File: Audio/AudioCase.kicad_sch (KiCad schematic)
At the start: 3 parts, among them J1 PD給電, J2 入力ジャック, J3 出力ジャック

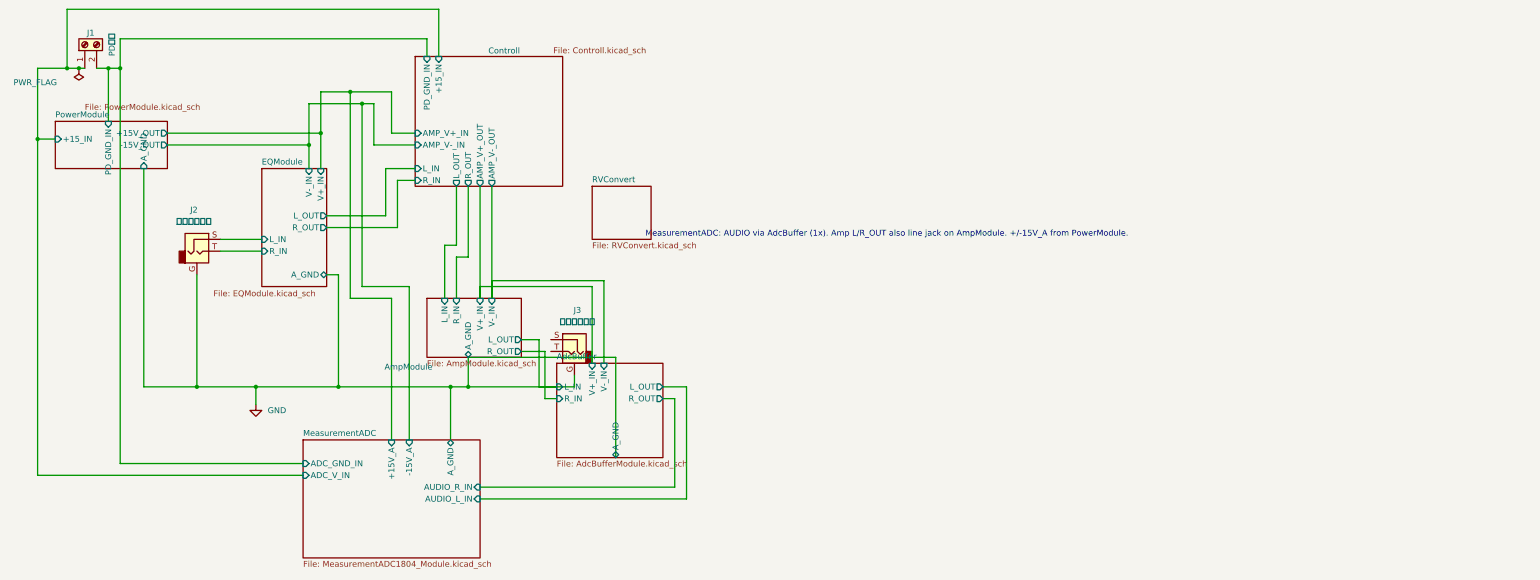
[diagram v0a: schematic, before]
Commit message: ヘッドホン出力と切替を追加し、S式検査をコミット前に走らせる。
Amp 後段を PHONE/MUTE/LINE に分け、NJM4556A の電流バッファとパッド付きボリュームを載せる。括弧崩れで回路図が開けなくなるのを check_sexpr と pre-commit で止める。

Co-authored-by: Cursor <cursoragent@cursor.com>
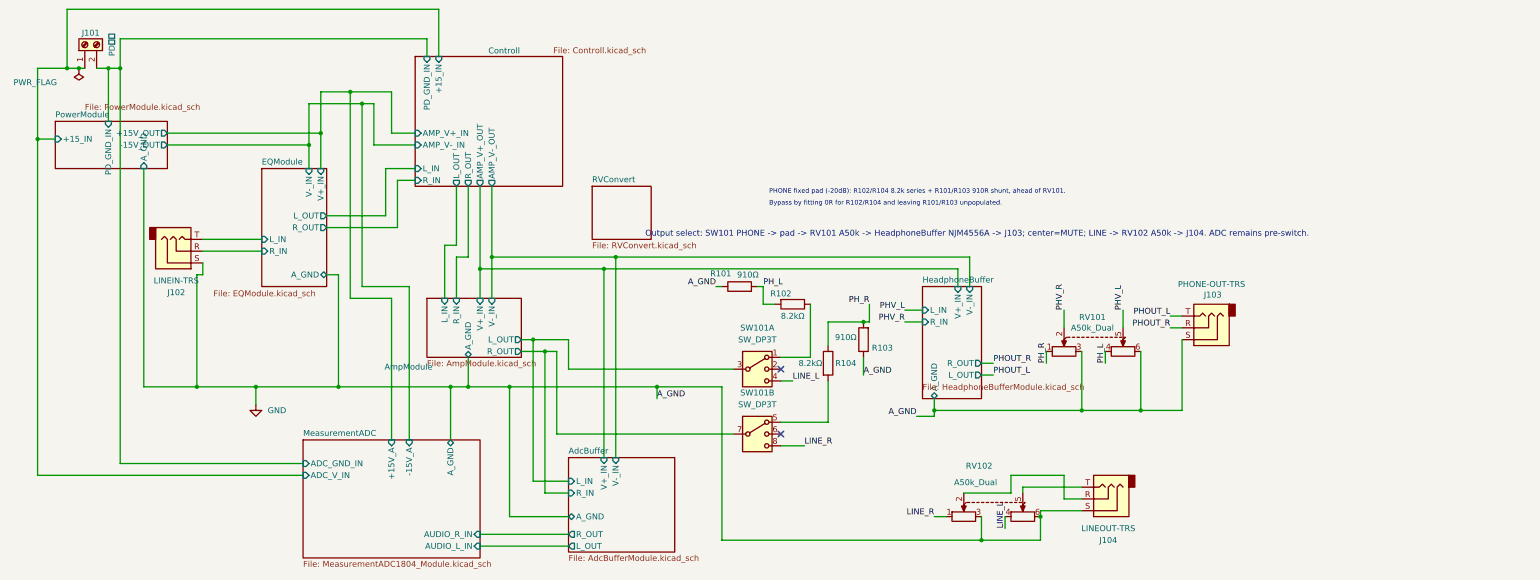
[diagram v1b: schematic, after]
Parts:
- removed J2: 入力ジャック, TerminalBlock_Phoenix:TerminalBlock_Phoenix_MKDS-1,5-2-5.08_1x02_P5.08mm_Horizontal, symbol Connector_Audio:AudioJack2_Ground
- added J102: LINEIN-TRS, Connector_Audio:Jack_3.5mm_CUI_SJ1-3523N_Horizontal, symbol Connector_Audio:AudioJack3
- added J103: PHONE-OUT-TRS, Connector_Audio:Jack_3.5mm_CUI_SJ1-3523N_Horizontal, symbol Connector_Audio:AudioJack3
- added R101, R103: 910Ω, Resistor_SMD:R_1206_3216Metric_Pad1.30x1.75mm_HandSolder, symbol Device:R
- added R102, R104: 8.2kΩ, Resistor_SMD:R_1206_3216Metric_Pad1.30x1.75mm_HandSolder, symbol Device:R
- added RV101, RV102: A50k_Dual, Potentiometer_THT:Potentiometer_Alps_RK097_Dual_Horizontal, symbol Device:R_Potentiometer_Dual
- added SW101: SW_DP3T, Connector_PinHeader_2.54mm:PinHeader_2x04_P2.54mm_Vertical, symbol Switch:SW_DP3T
- J104: renamed from J3; value 出力ジャック -> LINEOUT-TRS; footprint TerminalBlock_Phoenix:TerminalBlock_Phoenix_MKDS-1,5-2-5.08_1x02_P5.08mm_Horizontal -> Connector_Audio:Jack_3.5mm_CUI_SJ1-3523N_Horizontal; symbol Connector_Audio:AudioJack2_Ground -> Connector_Audio:AudioJack3
- renumbered J1 to J101
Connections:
- net AdcBuffer/R_IN: now also SW101.7
- net EQModule/L_IN: now also J102.T
- net EQModule/R_IN: now also J102.R
- net GND: now also J104.S, J102.S, J103.S, R101.1, R103.1, RV101.3, RV101.6, RV102.3, RV102.6; no longer J104.G
- net at J104.T: now also RV102.5
- new net: R102.1, SW101.1
- new net: J104.R, RV102.2
- new net: R104.2, SW101.5
- new net AdcBuffer/L_IN: SW101.3
- new net LINE_L: RV102.4, SW101.4
- new net LINE_R: RV102.1, SW101.8
- new net PHOUT_L: J103.T
- new net PHOUT_R: J103.R
- new net PHV_L: RV101.5
- new net PHV_R: RV101.2
- new net PH_L: R101.2, R102.2, RV101.4
- new net PH_R: R103.2, R104.1, RV101.1
- no-connect marks 0 -> 2
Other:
- added sheet HeadphoneBuffer (HeadphoneBufferModule.kicad_sch)
- note added: "Bypass by fitting 0R for R102/R104 and leaving R101/R103 unpopulated."
- note added: "Output select: SW101 PHONE -> pad -> RV101 A50k -> HeadphoneBuffer NJM4556A -> J103; center=MUTE; LINE -> RV102 A50k -> J104. ADC remains pre-switch."
- note added: "PHONE fixed pad (-20dB): R102/R104 8.2k series + R101/R103 910R shunt, ahead of RV101."
- note removed: "MeasurementADC: AUDIO via AdcBuffer (1x). Amp L/R_OUT also line jack on AmpModule. +/-15V_A from PowerModule."
